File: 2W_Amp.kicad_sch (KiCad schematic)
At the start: 42 parts, among them J1 Power_In, P1 SMA, P2 SMA, U1 OPA2674, U2 OPA2674

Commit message: some cleanup later...
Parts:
- P1, P2: footprint Connector_Coaxial:SMA_Amphenol_901-143_Horizontal -> Sma:SMA_PINS
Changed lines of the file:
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@@
 			)
 		)
-		(property "Footprint" "Connector_Coaxial:SMA_Amphenol_901-143_Horizontal"
+		(property "Footprint" "Sma:SMA_PINS"
 			(at 15.24 138.43 0)
 			(effects
@@
 			)
 		)
-		(property "Footprint" "Connector_Coaxial:SMA_Amphenol_901-143_Horizontal"
+		(property "Footprint" "Sma:SMA_PINS"
 			(at 208.28 129.54 0)
 			(effects

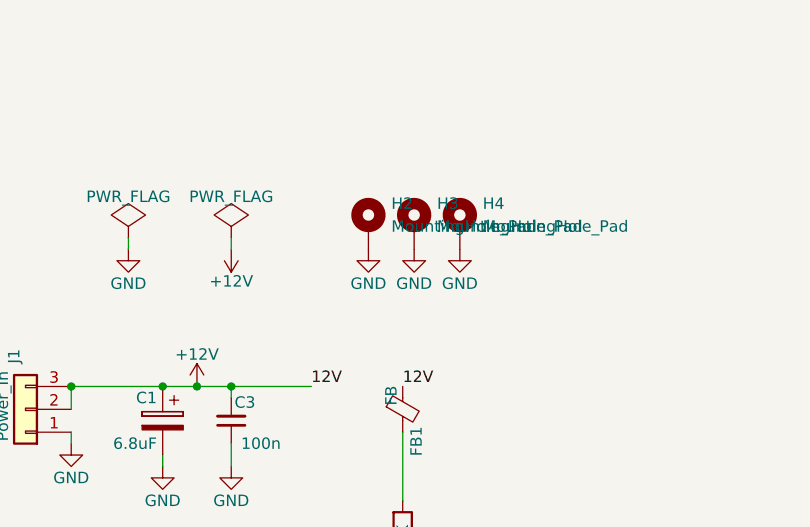
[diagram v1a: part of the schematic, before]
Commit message: decoupling on lower side, documentation added
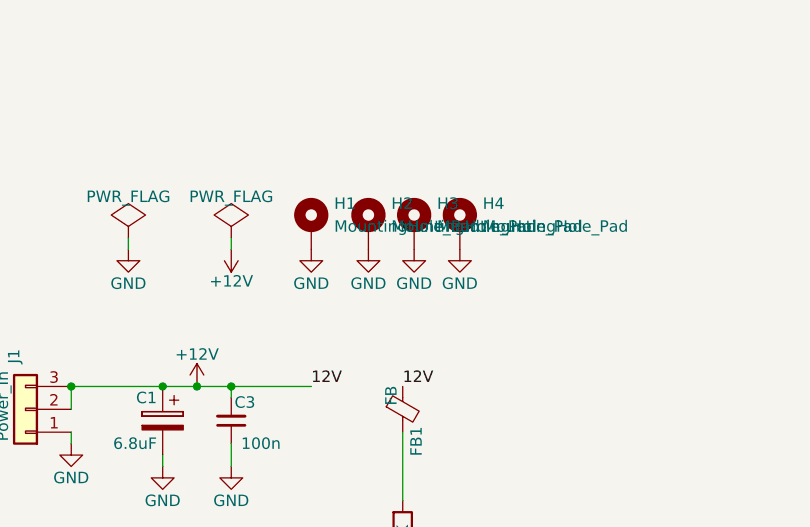
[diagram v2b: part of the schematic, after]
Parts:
- added H1: MountingHole_Pad, MountingHole:MountingHole_3.2mm_M3_DIN965_Pad_TopBottom, symbol Mechanical:MountingHole_Pad
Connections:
- net GND: now also H1.1
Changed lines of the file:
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@@
+	)
+	(symbol
+		(lib_id "Mechanical:MountingHole_Pad")
+		(at 46.99 86.36 0)
+		(unit 1)
+		(exclude_from_sim no)
+		(in_bom no)
+		(on_board yes)
+		(dnp no)
+		(fields_autoplaced yes)
+		(property "Reference" "H1"
+			(at 49.53 83.8199 0)
+			(effects
+				(font
+					(size 1.27 1.27)
+				)
+				(justify left)
+			)
+		)
+		(property "Value" "MountingHole_Pad"
+			(at 49.53 86.3599 0)
+			(effects
+				(font
+					(size 1.27 1.27)
+				)
+				(justify left)
+			)
+		)
+		(property "Footprint" "MountingHole:MountingHole_3.2mm_M3_DIN965_Pad_TopBottom"
+			(at 46.99 86.36 0)
+			(effects
+				(font
+					(size 1.27 1.27)
+				)
+				(hide yes)
+			)
+		)
+		(property "Datasheet" "~"
+			(at 46.99 86.36 0)
+			(effects
+				(font
+					(size 1.27 1.27)
+				)
+				(hide yes)
+			)
+		)
+		(property "Description" "Mounting Hole with connection"
+			(at 46.99 86.36 0)
+			(effects
+				(font
+					(size 1.27 1.27)
+				)
+				(hide yes)
+			)
+		)
+		(pin "1"
+		)
+		(instances
+			(project "2W_Amp"
+				(path "/7a822a47-5181-4908-833d-99bf896a3fd4"
+					(reference "H1")
+					(unit 1)
+				)
+			)
+		)
 	)
 	(symbol
@@
 					(unit 1)
 				)
+			)
+		)
+	)
+	(symbol
+		(lib_id "ampli1W-rescue:GND")
+		(at 46.99 88.9 0)
+		(mirror y)
+		(unit 1)
+		(exclude_from_sim no)
+		(in_bom yes)
+		(on_board yes)
+		(dnp no)
+		(property "Reference" "#PWR04"
+			(at 46.99 95.25 0)
+			(effects
+				(font
+					(size 1.27 1.27)
+				)
+				(hide yes)
+			)
+		)
+		(property "Value" "GND"
+			(at 46.99 92.71 0)
+			(effects
+				(font
+					(size 1.27 1.27)
+				)
+			)
+		)
+		(property "Footprint" ""
+			(at 46.99 88.9 0)
+			(effects
+				(font
+					(size 1.524 1.524)
+				)
+			)
+		)
+		(property "Datasheet" ""
+			(at 46.99 88.9 0)
+			(effects
+				(font
+					(size 1.524 1.524)
+				)
+			)
+		)
+		(property "Description" ""
+			(at 46.99 88.9 0)
+			(effects
+				(font
+					(size 1.27 1.27)
+				)
+				(hide yes)
+			)
+		)
+		(pin "1"
+		)
+		(instances
+			(project "2W_Amp"
+				(path "/7a822a47-5181-4908-833d-99bf896a3fd4"
+					(reference "#PWR04")
+					(unit 1)
+				)

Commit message: minor cosmetic changes
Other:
- note added: "1W RF Amplifier"
- note added: "Input power must not exceed 5 dBm"
- note added: "P out should not exceed 24 dBm (P in 0 dBm) for Pennywhistle P out should not exceed 26 dBm (P in 2 dBm) for Munin 100 LDMOS P out should be boosted at 32 dBm for Munin 400 LDMOS"
- note removed: "2W RF Amplifier"
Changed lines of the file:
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@@
 		)
 	)
-	(text "2W RF Amplifier"
+	(text "Input power must not exceed 5 dBm "
+		(exclude_from_sim no)
+		(at 64.77 24.13 0)
+		(effects
+			(font
+				(size 1.27 1.27)
+				(thickness 0.254)
+				(bold yes)
+				(color 255 15 15 1)
+			)
+		)
+	)
+	(text "1W RF Amplifier"
 		(exclude_from_sim no)
 		(at 158.496 67.564 0)
@@
 		)
 	)
+	(text "P out should not exceed 24 dBm (P in 0 dBm) for Pennywhistle\nP out should not exceed 26 dBm (P in 2 dBm) for Munin 100 LDMOS\nP out should be boosted at 32 dBm for Munin 400 LDMOS"
+		(exclude_from_sim no)
+		(at 46.99 19.05 0)
+		(effects
+			(font
+				(size 1.27 1.27)
+			)
+			(justify left)
+		)
+	)
